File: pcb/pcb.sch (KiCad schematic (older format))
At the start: 6 parts

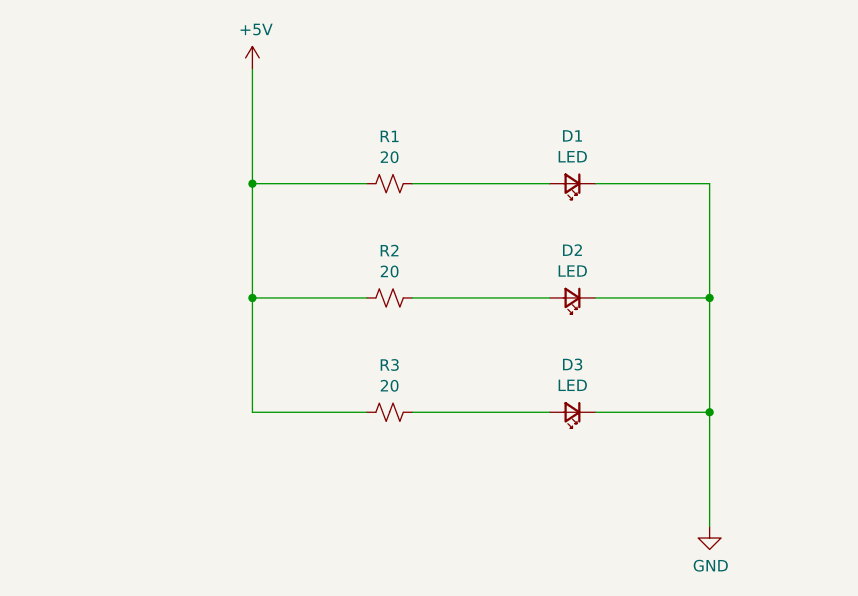
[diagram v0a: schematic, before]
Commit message: Add power flags
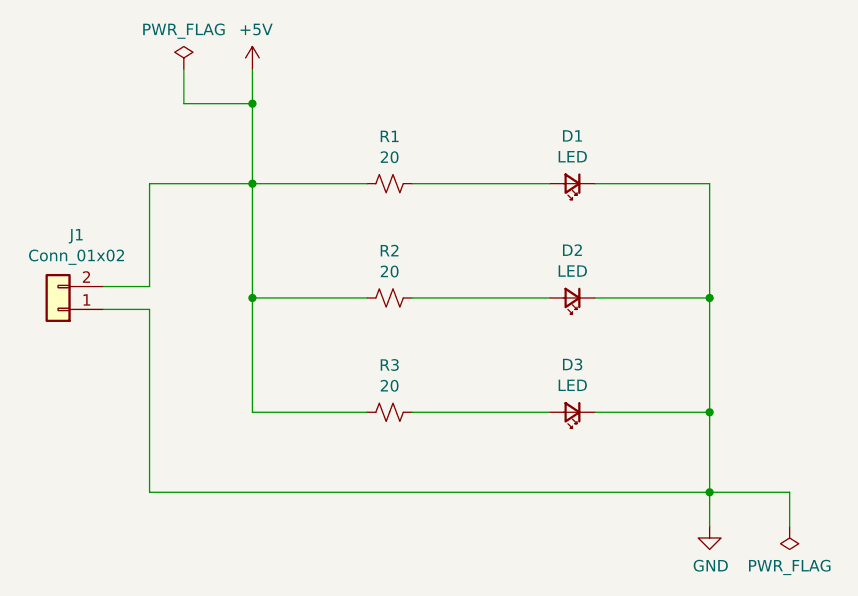
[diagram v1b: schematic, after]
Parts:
- added J1: Conn_01x02, Resistor_SMD:R_0805_2012Metric_Pad1.20x1.40mm_HandSolder, symbol Connector_Generic:Conn_01x02
- D1: footprint LED_SMD:LED_2816_7142Metric_Pad3.20x4.45mm_HandSolder -> LED_SMD:LED_0805_2012Metric_Pad1.15x1.40mm_HandSolder
- D2, D3: footprint LED_SMD:LED_2816_7142Metric_Pad3.20x4.45mm_HandSolder -> pcb:universal_LED
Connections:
- net +5V: now also J1.2 (Pin_2)
- net GND: now also J1.1 (Pin_1)
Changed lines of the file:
@@
 F 0 "D1" H 4900 2793 50  0000 C CNN
 F 1 "LED" H 4900 2884 50  0000 C CNN
-F 2 "LED_SMD:LED_2816_7142Metric_Pad3.20x4.45mm_HandSolder" V 4900 3000 50  0001 C CNN
+F 2 "LED_SMD:LED_0805_2012Metric_Pad1.15x1.40mm_HandSolder" V 4900 3000 50  0001 C CNN
 F 3 "~" V 4900 3000 50  0001 C CNN
 	1    4900 3000
@@
 F 0 "D2" H 4900 3293 50  0000 C CNN
 F 1 "LED" H 4900 3384 50  0000 C CNN
-F 2 "LED_SMD:LED_2816_7142Metric_Pad3.20x4.45mm_HandSolder" V 4900 3500 50  0001 C CNN
+F 2 "pcb:universal_LED" V 4900 3500 50  0001 C CNN
 F 3 "~" V 4900 3500 50  0001 C CNN
 	1    4900 3500
@@
 F 0 "D3" H 4900 3793 50  0000 C CNN
 F 1 "LED" H 4900 3884 50  0000 C CNN
-F 2 "LED_SMD:LED_2816_7142Metric_Pad3.20x4.45mm_HandSolder" V 4900 4000 50  0001 C CNN
+F 2 "pcb:universal_LED" V 4900 4000 50  0001 C CNN
 F 3 "~" V 4900 4000 50  0001 C CNN
 	1    4900 4000
@@
 $EndComp
 Wire Wire Line
-	3500 2500 3500 3000
+	3500 2500 3500 2650
 Wire Wire Line
 	3500 4000 4000 4000
@@
 Connection ~ 5500 4000
 Wire Wire Line
-	5500 4000 5500 4500
+	5500 4000 5500 4350
+$Comp
+L Connector_Generic:Conn_01x02 J1
+U 1 1 5FB2B626
+P 2650 3550
+F 0 "J1" H 2568 3225 50  0000 C CNN
+F 1 "Conn_01x02" H 2568 3316 50  0000 C CNN
+F 2 "Resistor_SMD:R_0805_2012Metric_Pad1.20x1.40mm_HandSolder" H 2650 3550 50  0001 C CNN
+F 3 "~" H 2650 3550 50  0001 C CNN
+	1    2650 3550
+	-1   0    0    1
+$EndComp
+Wire Wire Line
+	3500 3000 3050 3000
+Wire Wire Line
+	3050 3000 3050 3450
+Wire Wire Line
+	3050 3450 2850 3450
+Wire Wire Line
+	2850 3550 3050 3550
+Wire Wire Line
+	3050 3550 3050 4350
+Wire Wire Line
+	3050 4350 5500 4350
+Connection ~ 5500 4350
+Wire Wire Line
+	5500 4350 5500 4500
+$Comp
+L power:PWR_FLAG #FLG0101
+U 1 1 5FB375BE
+P 3200 2500
+F 0 "#FLG0101" H 3200 2575 50  0001 C CNN
+F 1 "PWR_FLAG" H 3200 2673 50  0000 C CNN
+F 2 "" H 3200 2500 50  0001 C CNN
+F 3 "~" H 3200 2500 50  0001 C CNN
+	1    3200 2500
+	1    0    0    -1
+$EndComp
+$Comp
+L power:PWR_FLAG #FLG0102
+U 1 1 5FB37B1E
+P 5850 4500
+F 0 "#FLG0102" H 5850 4575 50  0001 C CNN
+F 1 "PWR_FLAG" H 5850 4673 50  0000 C CNN
+F 2 "" H 5850 4500 50  0001 C CNN
+F 3 "~" H 5850 4500 50  0001 C CNN
+	1    5850 4500
+	-1   0    0    1
+$EndComp
+Wire Wire Line
+	3200 2500 3200 2650
+Wire Wire Line
+	3200 2650 3500 2650
+Connection ~ 3500 2650
+Wire Wire Line
+	3500 2650 3500 3000
+Wire Wire Line
+	5850 4500 5850 4350
+Wire Wire Line
+	5850 4350 5500 4350
 $EndSCHEMATC

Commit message: Go back to custom LED footprint (from testing one)
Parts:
- D1: footprint LED_SMD:LED_0805_2012Metric_Pad1.15x1.40mm_HandSolder -> pcb:universal_LED
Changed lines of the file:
@@
 F 0 "D1" H 4900 2793 50  0000 C CNN
 F 1 "LED" H 4900 2884 50  0000 C CNN
-F 2 "LED_SMD:LED_0805_2012Metric_Pad1.15x1.40mm_HandSolder" V 4900 3000 50  0001 C CNN
+F 2 "pcb:universal_LED" V 4900 3000 50  0001 C CNN
 F 3 "~" V 4900 3000 50  0001 C CNN
 	1    4900 3000

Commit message: Update capitalization
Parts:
- D1, D2, D3: footprint pcb:universal_LED -> pcb:Universal_LED
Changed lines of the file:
@@
 F 0 "D1" H 4900 2793 50  0000 C CNN
 F 1 "LED" H 4900 2884 50  0000 C CNN
-F 2 "pcb:universal_LED" V 4900 3000 50  0001 C CNN
+F 2 "pcb:Universal_LED" V 4900 3000 50  0001 C CNN
 F 3 "~" V 4900 3000 50  0001 C CNN
 	1    4900 3000
@@
 F 0 "D2" H 4900 3293 50  0000 C CNN
 F 1 "LED" H 4900 3384 50  0000 C CNN
-F 2 "pcb:universal_LED" V 4900 3500 50  0001 C CNN
+F 2 "pcb:Universal_LED" V 4900 3500 50  0001 C CNN
 F 3 "~" V 4900 3500 50  0001 C CNN
 	1    4900 3500
@@
 F 0 "D3" H 4900 3793 50  0000 C CNN
 F 1 "LED" H 4900 3884 50  0000 C CNN
-F 2 "pcb:universal_LED" V 4900 4000 50  0001 C CNN
+F 2 "pcb:Universal_LED" V 4900 4000 50  0001 C CNN
 F 3 "~" V 4900 4000 50  0001 C CNN
 	1    4900 4000

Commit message: Use new power connection
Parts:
- J1: footprint Resistor_SMD:R_0805_2012Metric_Pad1.20x1.40mm_HandSolder -> pcb:Power_Connection
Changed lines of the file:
@@
 F 0 "J1" H 2568 3225 50  0000 C CNN
 F 1 "Conn_01x02" H 2568 3316 50  0000 C CNN
-F 2 "Resistor_SMD:R_0805_2012Metric_Pad1.20x1.40mm_HandSolder" H 2650 3550 50  0001 C CNN
+F 2 "pcb:Power_Connection" H 2650 3550 50  0001 C CNN
 F 3 "~" H 2650 3550 50  0001 C CNN
 	1    2650 3550
